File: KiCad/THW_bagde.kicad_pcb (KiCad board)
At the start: 2 copper layers, 84.9 x 82.9 mm, 51 parts, among them J1 USB_B, J2 ISP, SW1 SW_Push, SW2 SW_Push, SW3 SW_Push, U1 ATmega328-P, Y1 Crystal

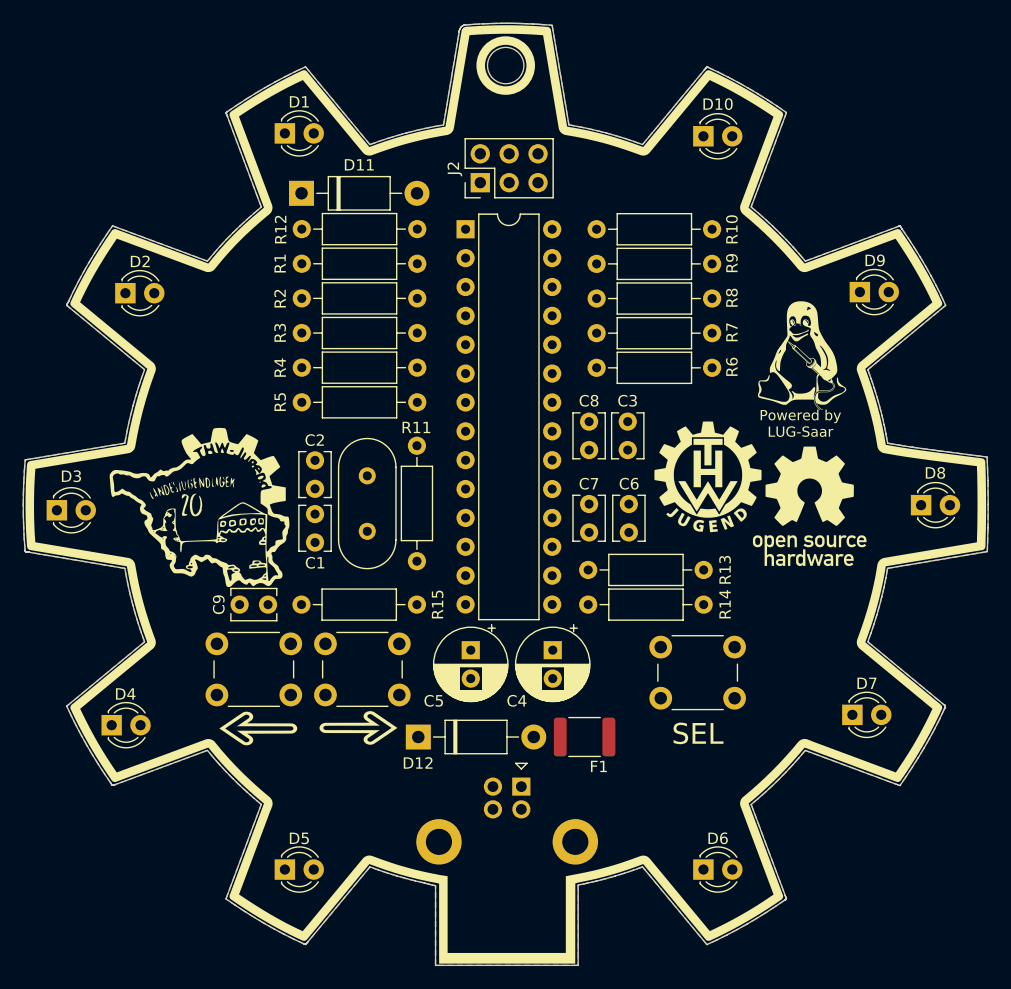
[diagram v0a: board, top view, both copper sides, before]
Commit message: Changing  user button circuit. Routing first components. Resize LUG logo in Drawing sheet.
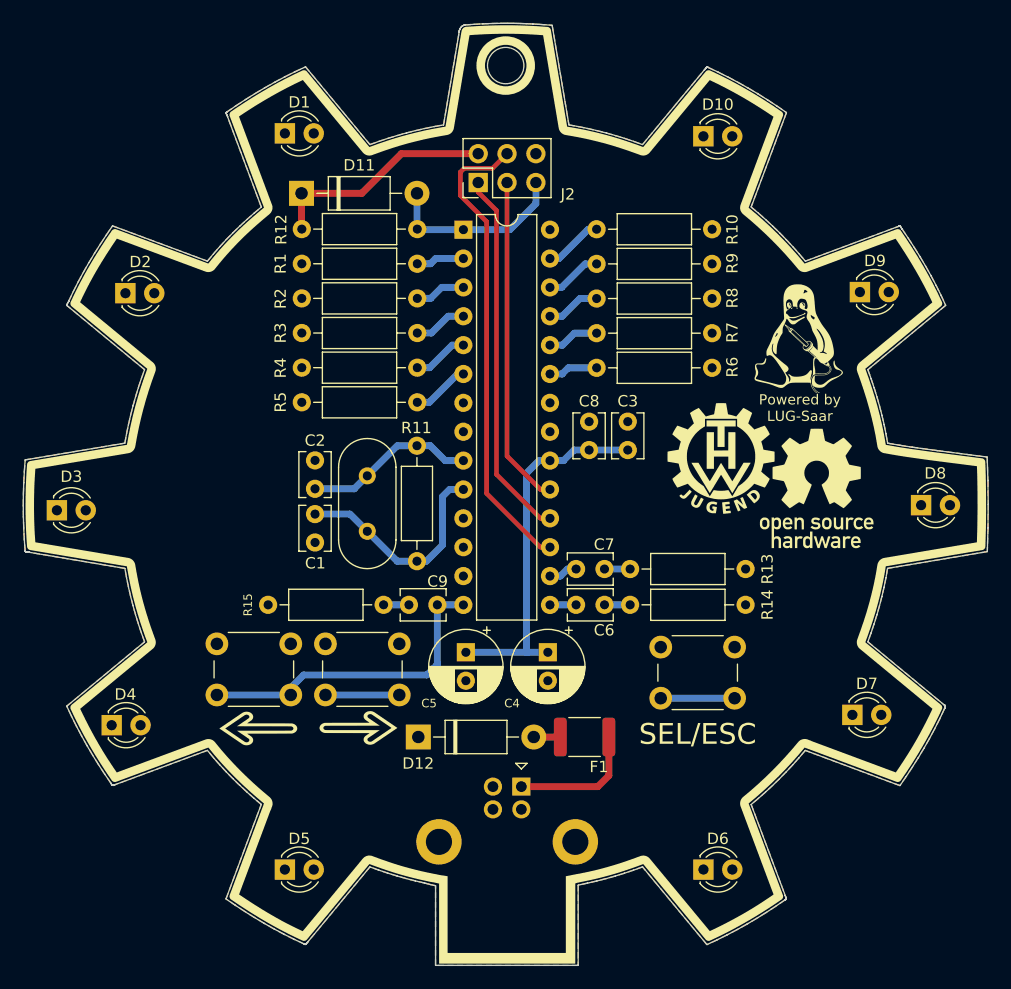
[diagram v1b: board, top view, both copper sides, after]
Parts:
- removed the G*** at (124.7, 91.8)
- C4, C5: value C_Polarized -> 100u
- C6, C7, C9: value C -> 100n
- R11: value R -> 1M
- R12: value 10k -> 10K
- R13, R14, R15: value 10k -> 100
- moved C9 17.4 mm to (145.5, 101.2), turned to 180 degrees
- moved C6 7.88 mm to (157.7, 101.2), turned to 0 degrees
- moved R13 3.69 mm to (172.6, 98.0)
- moved R14 3.69 mm to (172.6, 101.2)
- moved C7 3.42 mm to (157.7, 98.0), turned to 0 degrees
- moved R15 2.93 mm to (130.6, 101.2)
- moved G*** 1.99 mm to (170.5, 88.3)
- moved G*** 1.68 mm to (178.9, 90.9)
- moved G*** 1.52 mm to (177.3, 76.1)
- moved C5 0.47 mm to (148.0, 105.3)
- moved C4 0.47 mm to (155.2, 105.3)
- moved U1 0.20 mm to (147.8, 68.2)
- moved J2 0.19 mm to (149.1, 64.0)
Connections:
- C6 pad 2: GND -> Net-(R14-Pad2)
- C7 pad 2: GND -> Net-(C7-Pad2)
- C9 pad 2: GND -> Net-(C9-Pad2)
- R13 pad 2: /PB2 -> Net-(C7-Pad2)
- R14 pad 2: /PB1 -> Net-(R14-Pad2)
- R15 pad 2: /PB0 -> Net-(C9-Pad2)
- SW1 pad 1: +5V -> GND
- SW2 pad 1: +5V -> GND
- SW3 pad 1: +5V -> GND
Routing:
- net +5V: track 0.00 -> 53.0 mm
- net /MOSI: track 0.00 -> 41.5 mm
- net /MISO: track 0.00 -> 32.7 mm
- net /SCK: track 0.00 -> 29.1 mm
- net /PB0: track 0.00 -> 28.4 mm
- net Net-(C1-Pad1): track 0.00 -> 19.9 mm
- net /RES: track 0.00 -> 16.4 mm
- net Net-(C2-Pad1): track 0.00 -> 15.2 mm
- net Net-(F1-Pad1): track 0.00 -> 11.5 mm
- net /PB2: track 0.00 -> 9.05 mm
- net /PB1: track 0.00 -> 8.80 mm
- net /PC4: track 0.00 -> 5.17 mm
- net /PD4: track 0.00 -> 5.09 mm
- net /PC3: track 0.00 -> 4.96 mm
- net /PD3: track 0.00 -> 4.88 mm
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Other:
- board text added: "SEL/ESC"
- board text removed: "SEL"

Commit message: adding importent symbols
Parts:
- removed the G*** at (177.3, 76.1)
- removed the G*** at (178.9, 90.9)
- removed the G*** at (170.5, 88.3)
- added G***: LOGO, LOGO, F.Cu at (126.0, 87.6)
- added G***: LOGO, LOGO, F.Cu at (177.2, 81.3)
- added REF**: OSHW-Logo_5.7x6mm_SilkScreen, Symbol:OSHW-Logo_5.7x6mm_SilkScreen, F.Cu at (167.6, 85.6)
- added REF**: WEEE-Logo_4.2x6mm_SilkScreen, Symbol:WEEE-Logo_4.2x6mm_SilkScreen, F.Cu at (161.3, 92.3)
- added REF**: ESD-Logo_6.6x6mm_SilkScreen, Symbol:ESD-Logo_6.6x6mm_SilkScreen, F.Cu at (167.4, 92.4)
- J2: value ISP -> ICSP
- moved F1 0.45 mm to (158.9, 112.8)
- moved D12 0.38 mm to (144.2, 112.8)
- moved SW3 0.24 mm to (165.2, 104.7)
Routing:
- net +5V: track 53.0 -> 96.7 mm
- net /PB2: track 9.05 -> 35.5 mm
- net /PB1: track 8.80 -> 27.7 mm
- net /PB0: track 28.4 -> 27.7 mm

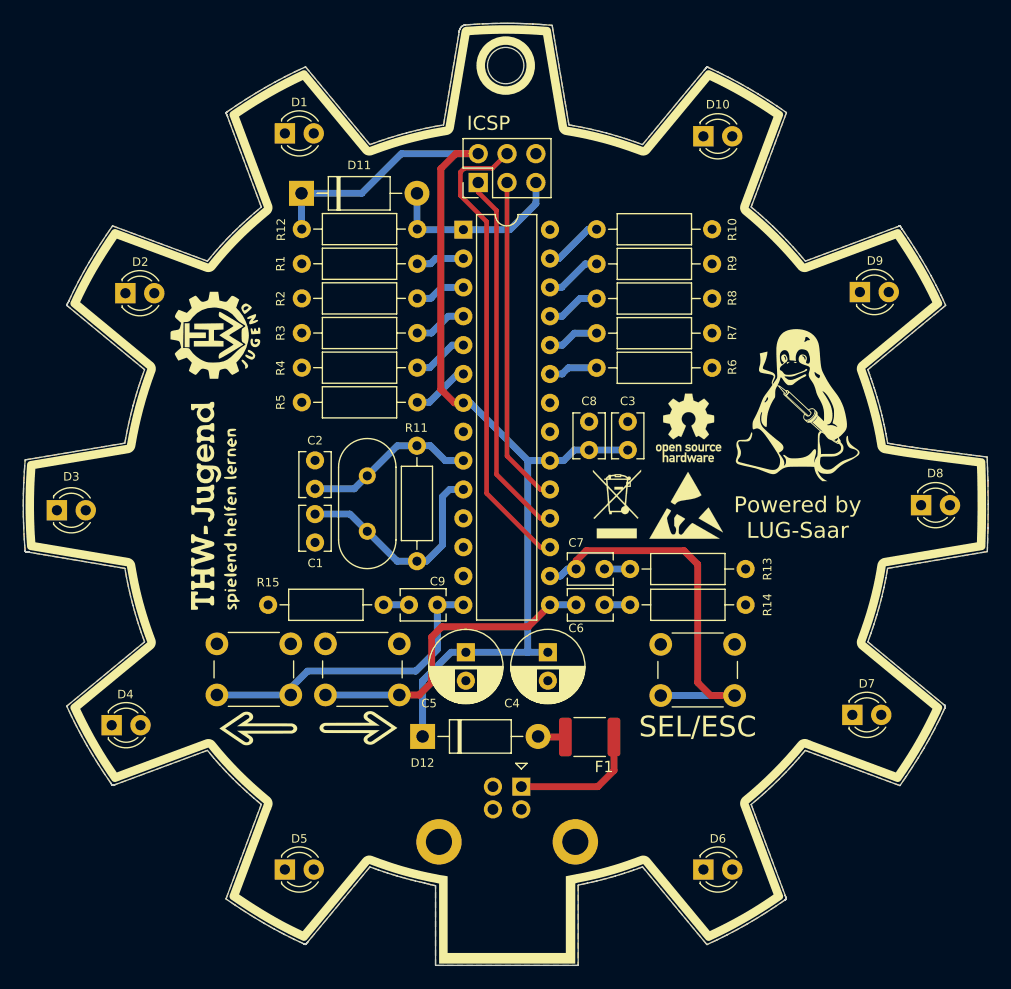
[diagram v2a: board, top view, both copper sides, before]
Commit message: routing LEDs
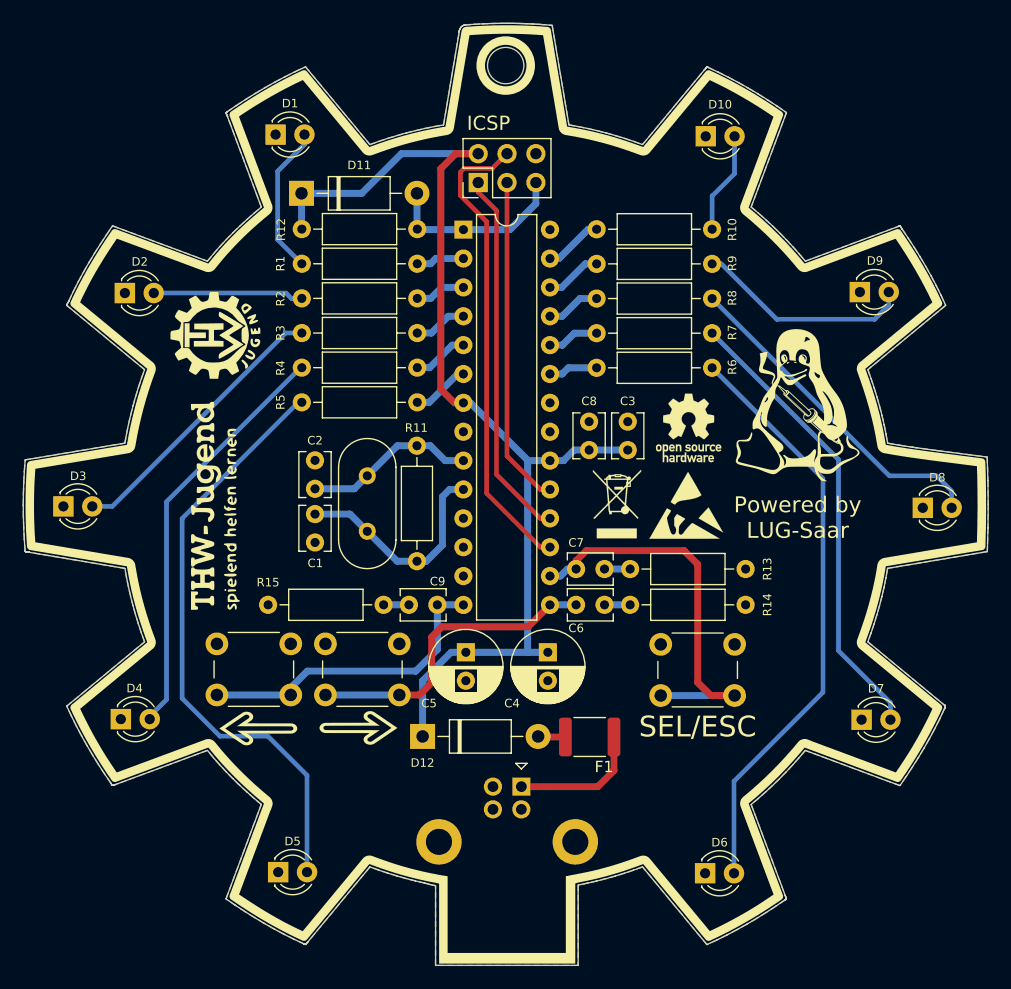
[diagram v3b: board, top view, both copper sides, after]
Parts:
- moved D4 0.97 mm to (117.6, 111.2)
- moved D7 0.92 mm to (182.8, 111.3)
- moved D1 0.82 mm to (131.3, 59.8)
- moved D3 0.67 mm to (112.6, 92.5)
- moved D5 0.63 mm to (131.5, 124.7)
- moved D6 0.36 mm to (169.1, 124.8)
- moved D8 0.28 mm to (188.2, 92.6)
- moved D10 0.20 mm to (169.1, 59.9)
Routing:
- net Net-(D5-Pad2): track 0.00 -> 52.9 mm
- net Net-(D6-Pad2): track 0.00 -> 51.8 mm
- net Net-(D7-Pad2): track 0.00 -> 40.5 mm
- net Net-(D4-Pad2): track 0.00 -> 36.5 mm
- net Net-(D8-Pad2): track 0.00 -> 29.6 mm
- net Net-(D3-Pad2): track 0.00 -> 24.8 mm
- net Net-(D9-Pad2): track 0.00 -> 19.2 mm
- net Net-(D1-Pad2): track 0.00 -> 13.2 mm
- net Net-(D2-Pad2): track 0.00 -> 13.2 mm
- net Net-(D10-Pad2): track 0.00 -> 9.00 mm
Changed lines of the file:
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@@
   )
   (footprint "LED_THT:LED_D3.0mm_Clear" (layer "F.Cu")
-    (at 112.02 92.85)
+    (at 112.5932 92.5068)
     (descr "IR-LED, diameter 3.0mm, 2 pins, color: clear")
     (tags "IR infrared LED diameter 3.0mm 2 pins clear")
@@
     (property "Sheetname" "")
     (attr through_hole)
-    (fp_text reference "D3" (at 1.27 -2.96) (layer "F.SilkS")
+    (fp_text reference "D3" (at 1.3004 -2.667) (layer "F.SilkS")
       (effects (font (size 0.75 0.75) (thickness 0.15)))
     )
@@
   )
   (footprint "LED_THT:LED_D3.0mm_Clear" (layer "F.Cu")
-    (at 132.08 59.69)
+    (at 131.2622 59.7916)
     (descr "IR-LED, diameter 3.0mm, 2 pins, color: clear")
     (tags "IR infrared LED diameter 3.0mm 2 pins clear")
@@
   )
   (footprint "LED_THT:LED_D3.0mm_Clear" (layer "F.Cu")
-    (at 188.06 92.4)
+    (at 188.209 92.6338)
     (descr "IR-LED, diameter 3.0mm, 2 pins, color: clear")
     (tags "IR infrared LED diameter 3.0mm 2 pins clear")
@@
     (property "Sheetname" "")
     (attr through_hole)
-    (fp_text reference "D8" (at 1.245 -2.802) (layer "F.SilkS")
+    (fp_text reference "D8" (at 1.275 -2.667) (layer "F.SilkS")
       (effects (font (size 0.75 0.75) (thickness 0.15)))
     )
@@
   )
   (footprint "LED_THT:LED_D3.0mm_Clear" (layer "F.Cu")
-    (at 118.05 73.75)
+    (at 118.0034 73.7362)
     (descr "IR-LED, diameter 3.0mm, 2 pins, color: clear")
     (tags "IR infrared LED diameter 3.0mm 2 pins clear")
@@
   )
   (footprint "LED_THT:LED_D3.0mm_Clear" (layer "F.Cu")
-    (at 168.91 124.46)
+    (at 169.0574 124.7902)
     (descr "IR-LED, diameter 3.0mm, 2 pins, color: clear")
     (tags "IR infrared LED diameter 3.0mm 2 pins clear")
@@
   )
   (footprint "LED_THT:LED_D3.0mm_Clear" (layer "F.Cu")
-    (at 182.015 110.85)
+    (at 182.8242 111.2774)
     (descr "IR-LED, diameter 3.0mm, 2 pins, color: clear")
     (tags "IR infrared LED diameter 3.0mm 2 pins clear")
@@
   )
   (footprint "LED_THT:LED_D3.0mm_Clear" (layer "F.Cu")
-    (at 132.08 124.46)
+    (at 131.4908 124.6886)
     (descr "IR-LED, diameter 3.0mm, 2 pins, color: clear")
     (tags "IR infrared LED diameter 3.0mm 2 pins clear")
@@
   )
   (footprint "LED_THT:LED_D3.0mm_Clear" (layer "F.Cu")
-    (at 116.84 111.76)
+    (at 117.6478 111.2266)
     (descr "IR-LED, diameter 3.0mm, 2 pins, color: clear")
     (tags "IR infrared LED diameter 3.0mm 2 pins clear")
@@
   )
   (footprint "LED_THT:LED_D3.0mm_Clear" (layer "F.Cu")
-    (at 168.905 59.944)
+    (at 169.1082 59.944)
     (descr "IR-LED, diameter 3.0mm, 2 pins, color: clear")
     (tags "IR infrared LED diameter 3.0mm 2 pins clear")
@@
   (segment (start 143.6972 87.1728) (end 143.7 87.17) (width 0.6096) (layer "B.Cu") (net 2))
   (segment (start 138.1912 90.96) (end 139.3312 89.82) (width 0.6096) (layer "B.Cu") (net 2))
+  (segment (start 131.445 69.0372) (end 133.5658 71.158) (width 0.4064) (layer "B.Cu") (net 3))
+  (segment (start 133.5658 71.158) (end 133.57 71.158) (width 0.4064) (layer "B.Cu") (net 3))
+  (segment (start 131.445 63.0174) (end 131.445 69.0372) (width 0.4064) (layer "B.Cu") (net 3))
+  (segment (start 133.8022 60.6602) (end 131.445 63.0174) (width 0.4064) (layer "B.Cu") (net 3))
+  (segment (start 133.8022 59.7916) (end 133.8022 60.6602) (width 0.4064) (layer "B.Cu") (net 3))
+  (segment (start 132.1816 73.7362) (end 120.5434 73.7362) (width 0.4064) (layer "B.Cu") (net 4))
+  (segment (start 133.57 74.206) (end 132.6514 74.206) (width 0.4064) (layer "B.Cu") (net 4))
+  (segment (start 132.6514 74.206) (end 132.1816 73.7362) (width 0.4064) (layer "B.Cu") (net 4))
+  (segment (start 115.1332 92.5068) (end 116.8908 92.5068) (width 0.4064) (layer "B.Cu") (net 5))
+  (segment (start 132.1436 77.254) (end 133.57 77.254) (width 0.4064) (layer "B.Cu") (net 5))
+  (segment (start 116.8908 92.5068) (end 132.1436 77.254) (width 0.4064) (layer "B.Cu") (net 5))
+  (segment (start 120.1878 110.9776) (end 120.1878 111.2266) (width 0.4064) (layer "B.Cu") (net 6))
+  (segment (start 121.666 92.1004) (end 121.666 109.4994) (width 0.4064) (layer "B.Cu") (net 6))
+  (segment (start 133.4644 80.302) (end 121.666 92.1004) (width 0.4064) (layer "B.Cu") (net 6))
+  (segment (start 133.57 80.302) (end 133.4644 80.302) (width 0.4064) (layer "B.Cu") (net 6))
+  (segment (start 121.666 109.4994) (end 120.1878 110.9776) (width 0.4064) (layer "B.Cu") (net 6))
+  (segment (start 134.0308 124.6886) (end 134.0308 116.1746) (width 0.4064) (layer "B.Cu") (net 7))
+  (segment (start 123.0376 109.3978) (end 123.0376 93.5736) (width 0.4064) (layer "B.Cu") (net 7))
+  (segment (start 123.0376 93.5736) (end 133.2612 83.35) (width 0.4064) (layer "B.Cu") (net 7))
+  (segment (start 126.365 112.7252) (end 123.0376 109.3978) (width 0.4064) (layer "B.Cu") (net 7))
+  (segment (start 134.0308 116.1746) (end 130.5814 112.7252) (width 0.4064) (layer "B.Cu") (net 7))
+  (segment (start 130.5814 112.7252) (end 126.365 112.7252) (width 0.4064) (layer "B.Cu") (net 7))
+  (segment (start 133.2612 83.35) (end 133.57 83.35) (width 0.4064) (layer "B.Cu") (net 7))
+  (segment (start 179.4256 90.0684) (end 179.4256 108.8644) (width 0.4064) (layer "B.Cu") (net 8))
+  (segment (start 169.672 80.3148) (end 179.4256 90.0684) (width 0.4064) (layer "B.Cu") (net 8))
+  (segment (start 179.4256 108.8644) (end 171.5974 116.6926) (width 0.4064) (layer "B.Cu") (net 8))
+  (segment (start 171.5974 116.6926) (end 171.5974 124.7902) (width 0.4064) (layer "B.Cu") (net 8))
+  (segment (start 180.7972 105.2068) (end 185.3642 109.7738) (width 0.4064) (layer "B.Cu") (net 9))
+  (segment (start 185.3642 109.7738) (end 185.3642 111.2774) (width 0.4064) (layer "B.Cu") (net 9))
+  (segment (start 169.672 77.2668) (end 180.7972 88.392) (width 0.4064) (layer "B.Cu") (net 9))
+  (segment (start 180.7972 88.392) (end 180.7972 105.2068) (width 0.4064) (layer "B.Cu") (net 9))
+  (segment (start 189.4078 89.8144) (end 190.749 91.1556) (width 0.4064) (layer "B.Cu") (net 10))
+  (segment (start 185.2676 89.8144) (end 189.4078 89.8144) (width 0.4064) (layer "B.Cu") (net 10))
+  (segment (start 169.672 74.2188) (end 185.2676 89.8144) (width 0.4064) (layer "B.Cu") (net 10))
+  (segment (start 190.749 91.1556) (end 190.749 92.6338) (width 0.4064) (layer "B.Cu") (net 10))
+  (segment (start 175.3616 76.0476) (end 183.9722 76.0476) (width 0.4064) (layer "B.Cu") (net 11))
+  (segment (start 185.215 74.8048) (end 185.215 73.65) (width 0.4064) (layer "B.Cu") (net 11))
+  (segment (start 170.4848 71.1708) (end 175.3616 76.0476) (width 0.4064) (layer "B.Cu") (net 11))
+  (segment (start 183.9722 76.0476) (end 185.215 74.8048) (width 0.4064) (layer "B.Cu") (net 11))
+  (segment (start 169.672 71.1708) (end 170.4848 71.1708) (width 0.4064) (layer "B.Cu") (net 11))
+  (segment (start 171.6482 63.2256) (end 169.672 65.2018) (width 0.4064) (layer "B.Cu") (net 12))
+  (segment (start 171.6482 59.944) (end 171.6482 63.2256) (width 0.4064) (layer "B.Cu") (net 12))
+  (segment (start 169.672 65.2018) (end 169.672 68.1228) (width 0.4064) (layer "B.Cu") (net 12))
   (segment (start 144.8944 71.158) (end 143.73 71.158) (width 0.6096) (layer "B.Cu") (net 13))
   (segment (start 147.7872 70.6982) (end 145.3542 70.6982) (width 0.6096) (layer "B.Cu") (net 13))
